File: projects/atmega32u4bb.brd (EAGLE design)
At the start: 50.8 x 50.9 mm, 32 parts, among them CN1 MiniB USB, IC1 ATMEGA32U4-AU, X3 16MHz

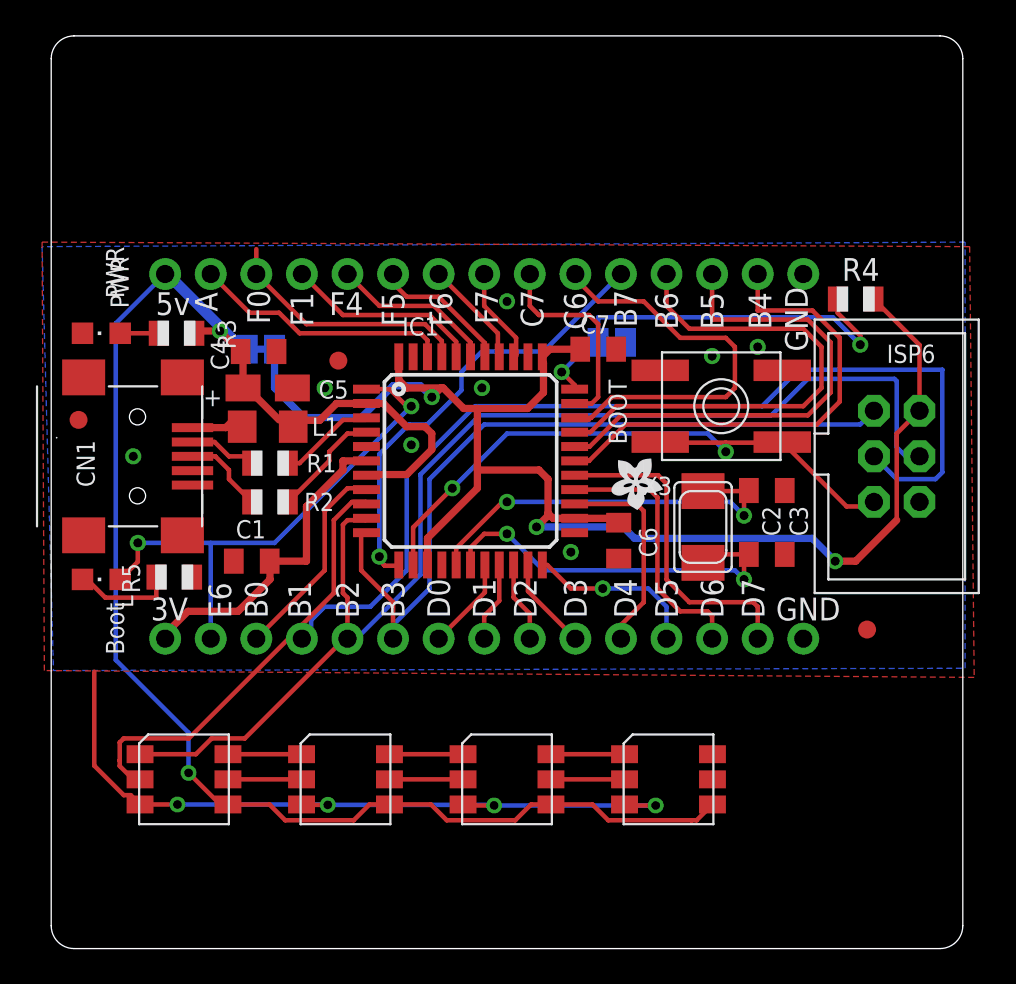
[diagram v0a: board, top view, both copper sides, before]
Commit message: Add 2020 (2mm by 2mm) footprint for dotstar, updated example to use that footprint
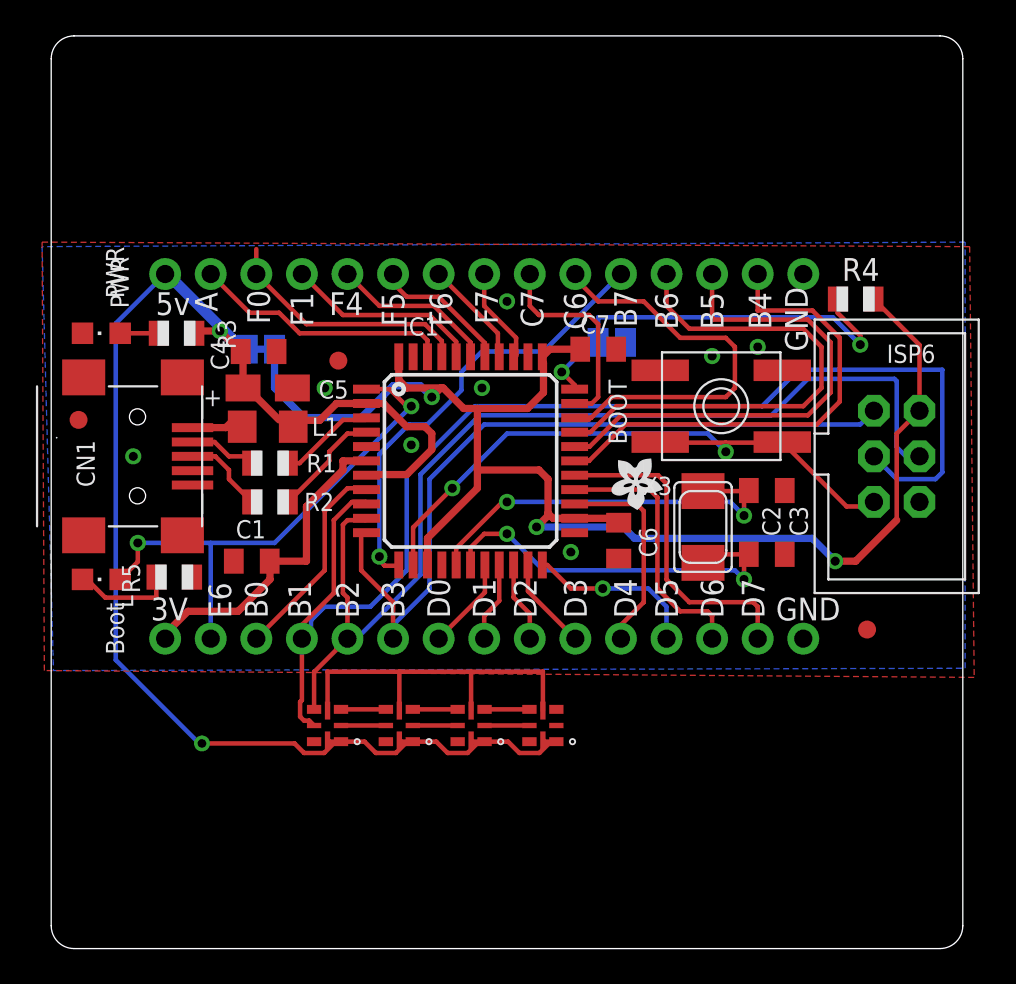
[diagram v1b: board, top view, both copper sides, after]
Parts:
- U$3, U$5, U$7, U$8: value DOTSTAR -> DOTSTAR2020; device codenext2020:SK9822 -> codenext2020:LED_3341
- moved U$3 8.54 mm to (16.0, 12.0)
- moved U$8 7.62 mm to (28.0, 12.0)
- moved U$5 4.24 mm to (20.0, 12.0)
- moved U$7 3.61 mm to (24.0, 12.0)
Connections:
- net +5V: now also U$3.1, U$3.8, U$5.1, U$5.8, U$7.1, U$7.8, U$8.1, U$8.8; no longer U$3.VCC, U$5.VCC, U$7.VCC, U$8.VCC
- net GND: now also U$3.6, U$3.7, U$5.6, U$5.7, U$7.6, U$7.7, U$8.6, U$8.7; no longer U$3.GND, U$5.GND, U$7.GND, U$8.GND
- net MOSI: now also U$3.4; no longer U$3.SDI
- net N$11: now also U$3.3, U$5.4; no longer U$3.SDO, U$5.SDI
- net N$12: now also U$3.2, U$5.5; no longer U$3.CKO, U$5.CKI
- net N$13: now also U$5.3, U$7.4; no longer U$5.SDO, U$7.SDI
- net N$14: now also U$5.2, U$7.5; no longer U$5.CKO, U$7.CKI
- net N$15: now also U$7.3, U$8.4; no longer U$7.SDO, U$8.SDI
- net N$16: now also U$7.2, U$8.5; no longer U$7.CKO, U$8.CKI
- net SCK: now also U$3.5; no longer U$3.CKI
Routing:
- net GND: track 43.6 -> 21.8 mm, vias 12 -> 8
- net SCK: track 80.5 -> 71.3 mm
- net MOSI: track 67.3 -> 58.6 mm
- net +5V: track 94.9 -> 86.3 mm
- net N$14: track 4.10 -> 2.50 mm
- net N$13: track 4.10 -> 2.50 mm
- net N$12: track 4.10 -> 2.50 mm
- net N$11: track 4.10 -> 2.50 mm
- net N$16: track 4.10 -> 2.50 mm
- net N$15: track 4.10 -> 2.50 mm
